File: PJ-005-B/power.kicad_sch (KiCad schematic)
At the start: 41 parts, among them J1 2 Pin JST XH, J2 2 Pin JST XH, U1 MIC29302WU-TR, U2 MIC29302WU-TR, U3 MIC29302WU-TR, U4 LM337IMP/NOPB, U5 REF2033AIDDCR, U6 MIC5365-2.5YC5-TR

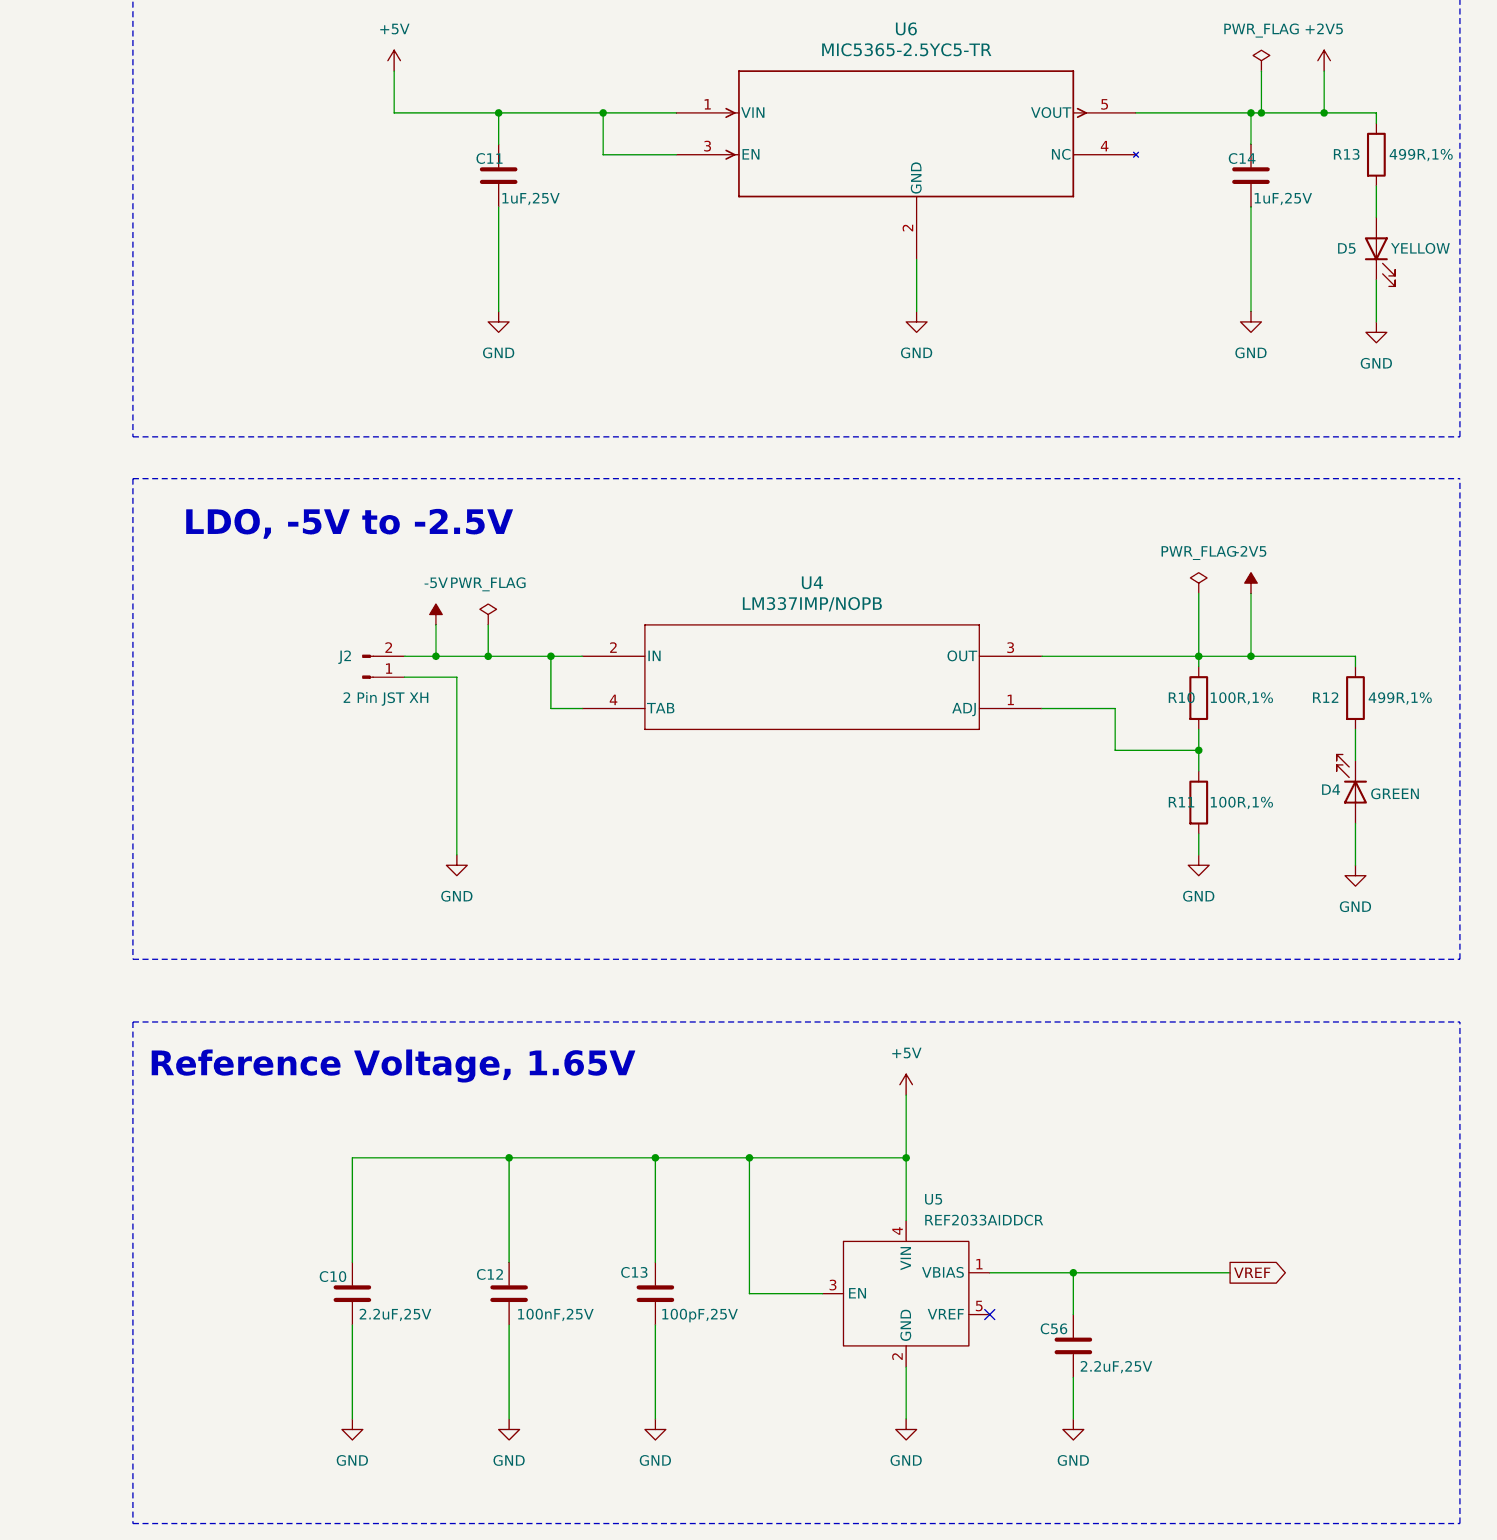
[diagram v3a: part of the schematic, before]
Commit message: Transceiver After Review
-- Added bulk capacitors for -2.5V LDO
-- Added 0R for shorting RE and DE in TTL to RS485
-- Changed the snubber values in transformer primary to 2.2nF and 33R
-- Removed the 10nF and 100K in parallel with the transducer
-- Added 1000uF capacitor for transformer centre tap
-- Added 100pF decoupling capacitor for gate driver IC
--Changed secondary snubber values to 220nF and 680R
-- Changed LC inductor value to 100uH (transformer secondary)
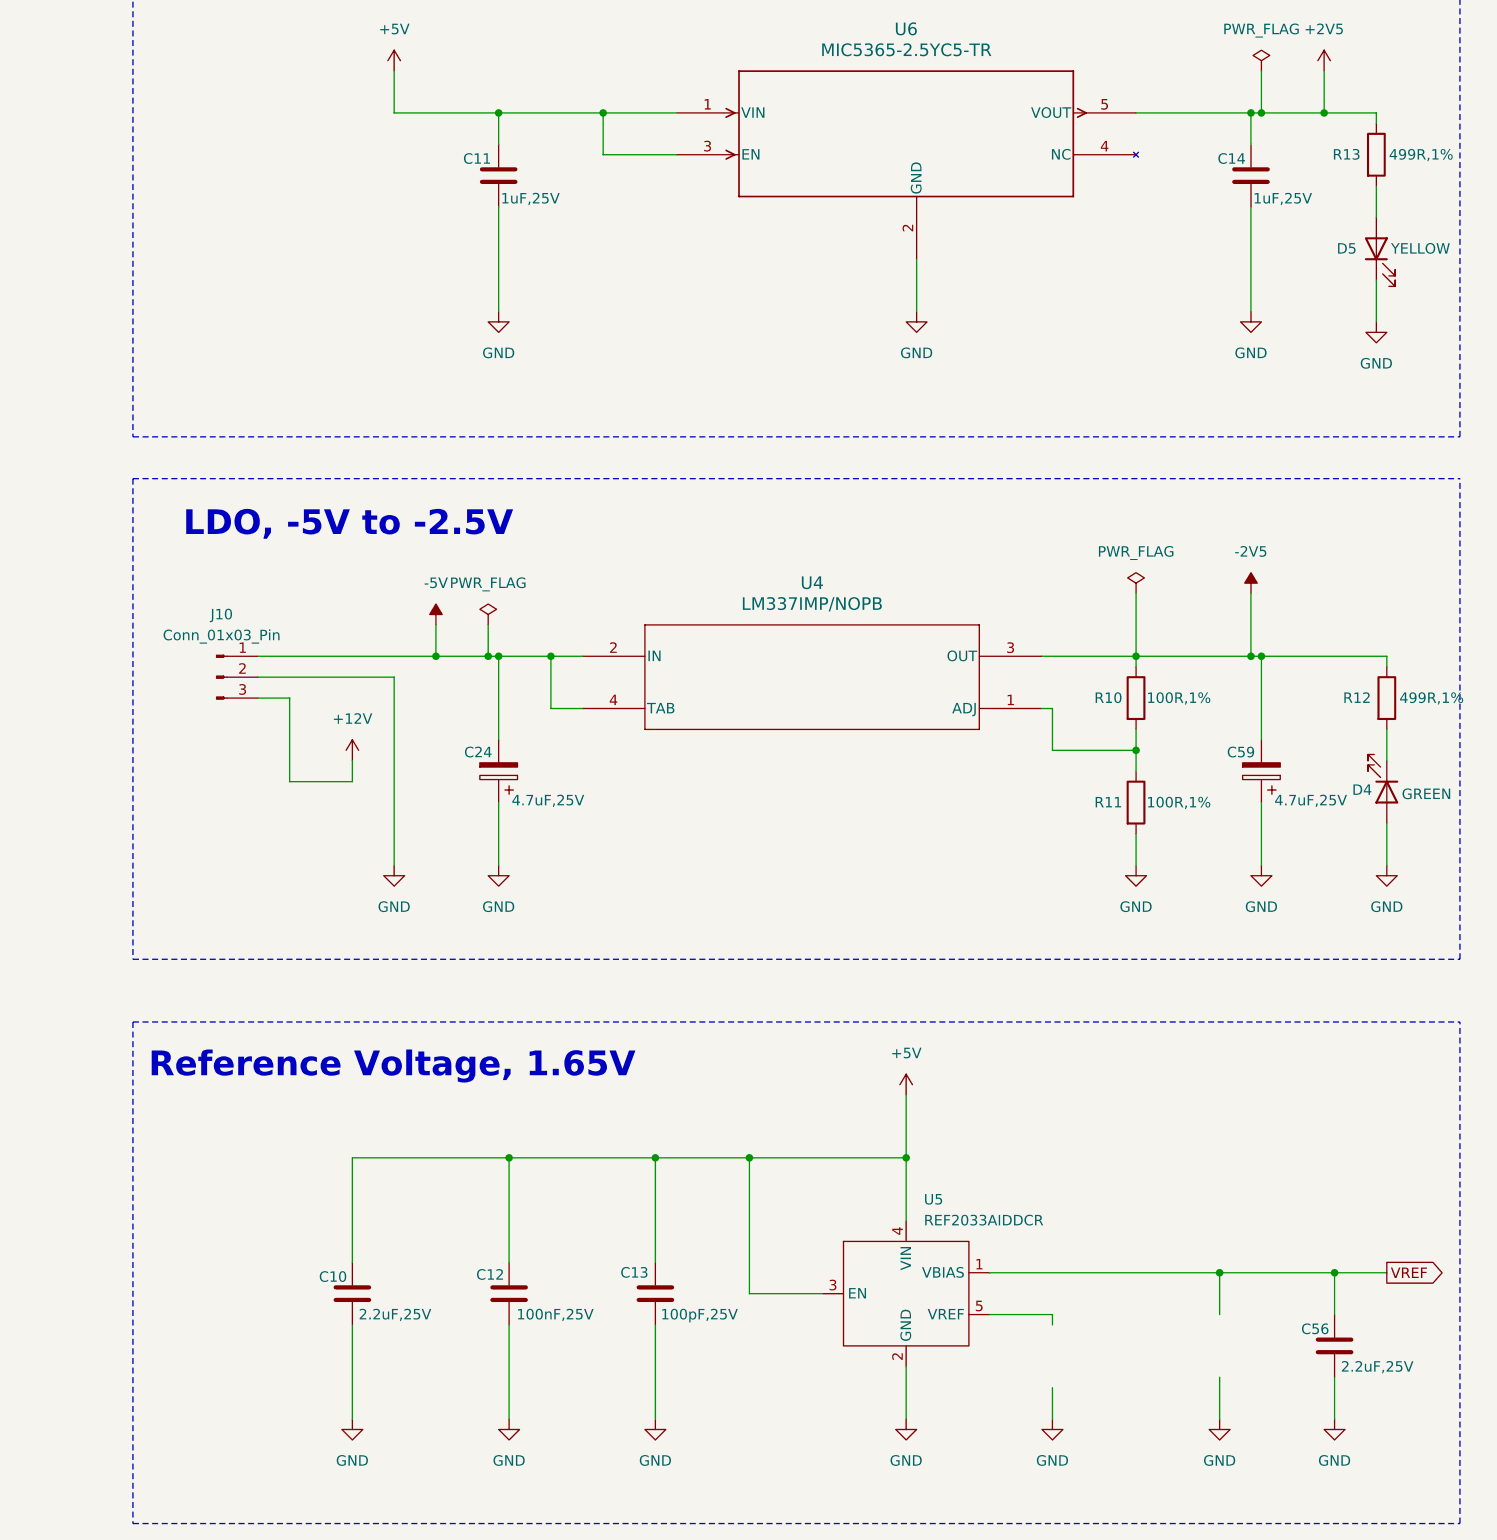
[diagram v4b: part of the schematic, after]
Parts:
- removed J2: 2 Pin JST XH, Connector_JST:JST_XH_B2B-XH-A_1x02_P2.50mm_Vertical, symbol Connector:Conn_01x02_Pin
- added C24, C59: 4.7uF,25V, XaltenFootprints:C1206, symbol Device:C_Polarized
- added J10: Conn_01x03_Pin, symbol Connector:Conn_01x03_Pin
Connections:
- net +12V: now also J10.3 (Pin_3)
- net -2V5: now also C59.2
- net -5V: now also C24.2, J10.1 (Pin_1)
- net GND: now also C24.1, C59.1, J10.2 (Pin_2)
- no-connect marks 1 -> 0
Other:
- moved on the sheet: C56, D4, R10, R11, R12

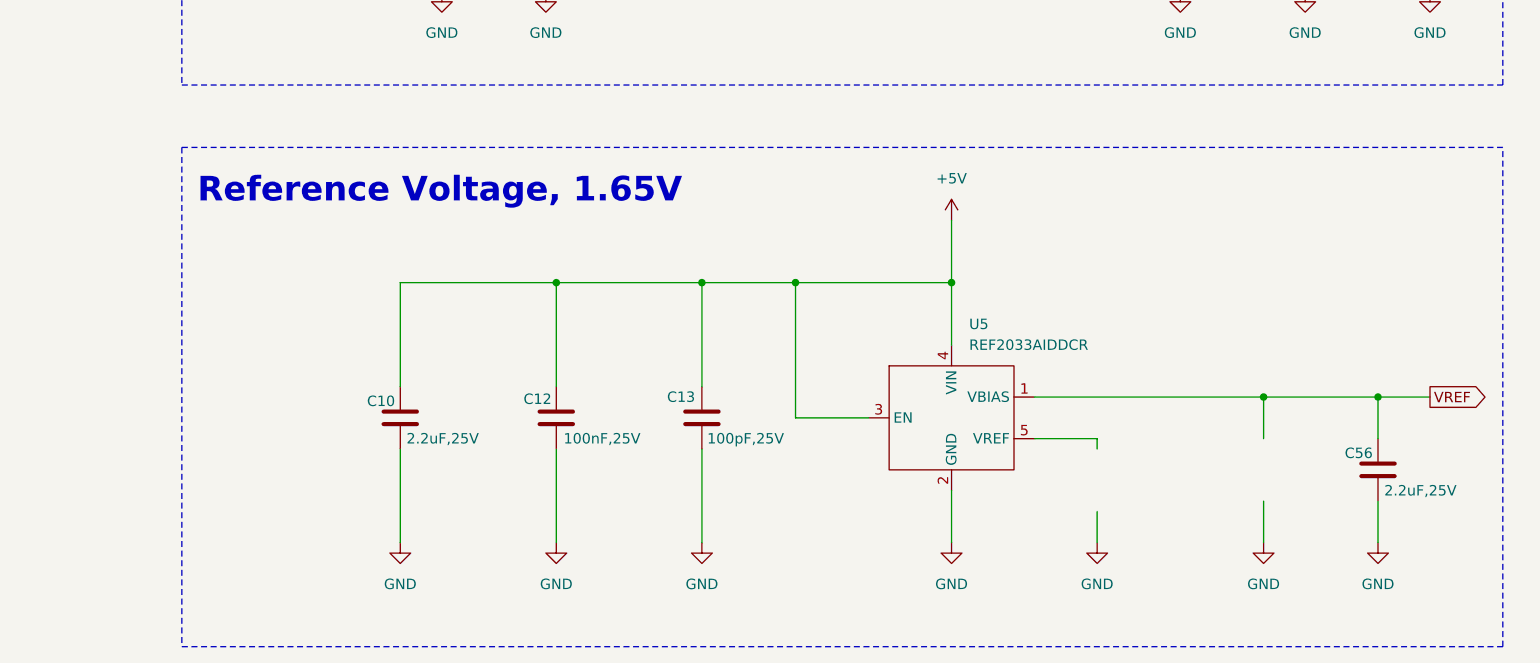
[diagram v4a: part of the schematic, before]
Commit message: -- Reference Voltage IC removed -- Receiver includes only transmit receive switch and charge amp -- Changes in snubber values -- Changes in pull-up and pull-down resistors
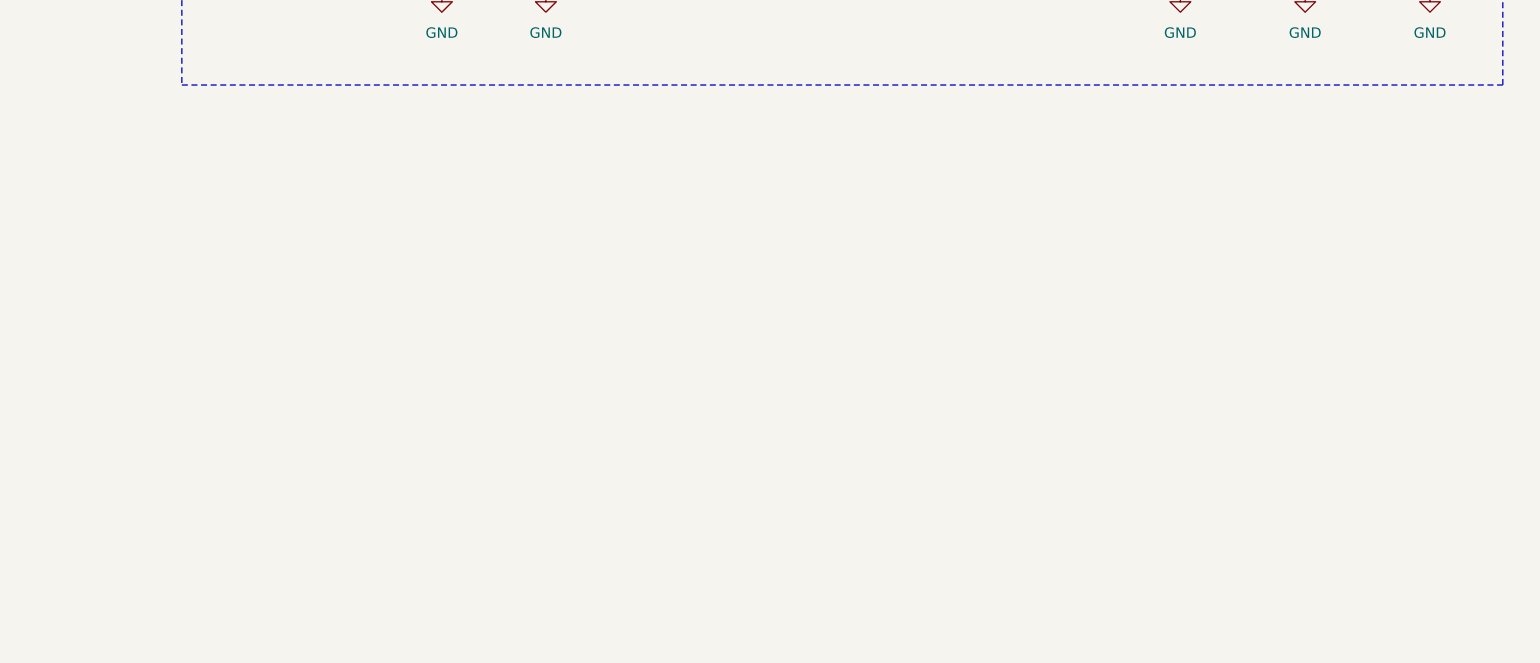
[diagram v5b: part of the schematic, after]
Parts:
- removed C10, C56: 2.2uF,25V, XaltenFootprints:C0603, symbol Device:C
- removed C12: 100nF,25V, XaltenFootprints:C0603, symbol Device:C
- removed C13: 100pF,25V, XaltenFootprints:C0603, symbol Device:C
- removed U5: REF2033AIDDCR, XaltenFootprints:SOT-23-5, symbol Echosounder Transceiver:REF2033AIDDCR
- J10: footprint (none) -> Connector_PinHeader_2.54mm:PinHeader_1x03_P2.54mm_Vertical
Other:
- note removed: "Reference Voltage, 1.65V"
